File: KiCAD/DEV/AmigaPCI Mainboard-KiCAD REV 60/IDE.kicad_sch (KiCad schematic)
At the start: 55 parts, among them CN900 PRIMARY IDE, CN901 SECONDARY IDE, Q900 MMBT3906, U220 74LVC08, U815 74LVC08, U900 74LVC245, U901 74LVC245, U902 74LVC245, U903 74LVC245, U904 74LVC245, U905 74LVC245, U906 74LVC373, U907 74LVC373

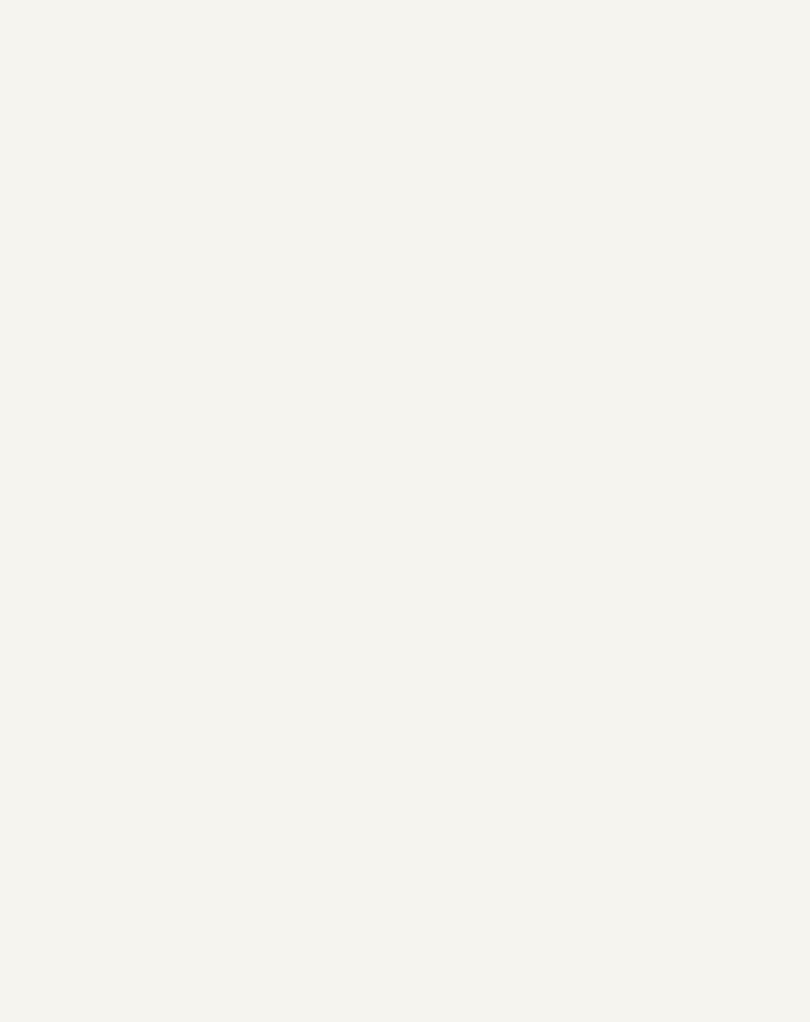
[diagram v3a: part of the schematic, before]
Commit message: Rev 6.0 APCI Work
Added ATA address lines to U110.
Cleaned up some routing.
Removed address lines from U109 - we can pick them up from the AD bus.
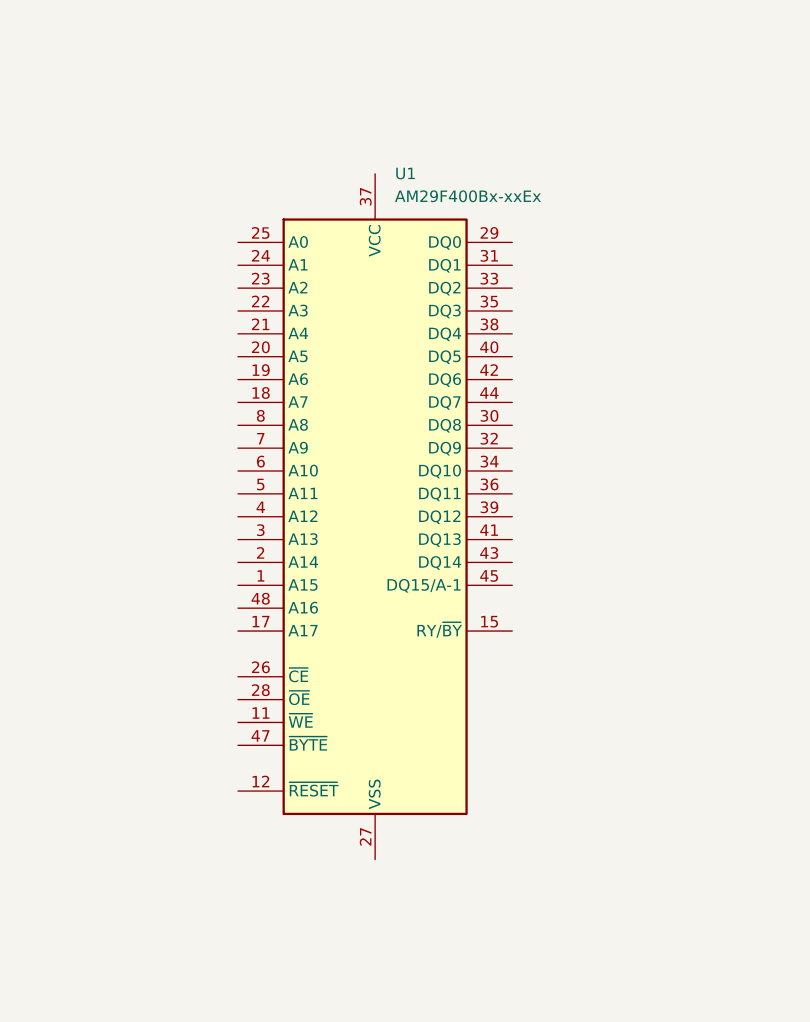
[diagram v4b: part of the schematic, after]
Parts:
- added U1: AM29F400Bx-xxEx, Package_SO:TSOP-I-48_18.4x12mm_P0.5mm, symbol Memory_Flash:AM29F400Bx-xxEx
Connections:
- new net: U1.27 (VSS), U1.46 (VSS)
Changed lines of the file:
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@@
+	)
+	(symbol
+		(lib_id "Memory_Flash:AM29F400Bx-xxEx")
+		(at 278.13 172.72 0)
+		(unit 1)
+		(exclude_from_sim no)
+		(in_bom yes)
+		(on_board yes)
+		(dnp no)
+		(fields_autoplaced yes)
+		(property "Reference" "U1"
+			(at 280.3241 134.62 0)
+			(effects
+				(font
+					(size 1.27 1.27)
+				)
+				(justify left)
+			)
+		)
+		(property "Value" "AM29F400Bx-xxEx"
+			(at 280.3241 137.16 0)
+			(effects
+				(font
+					(size 1.27 1.27)
+				)
+				(justify left)
+			)
+		)
+		(property "Footprint" "Package_SO:TSOP-I-48_18.4x12mm_P0.5mm"
+			(at 278.13 172.72 0)
+			(effects
+				(font
+					(size 1.27 1.27)
+				)
+				(hide yes)
+			)
+		)
+		(property "Datasheet" "https://www.mouser.com/datasheet/2/380/AM29F400B_EOL_21505e8-9219.pdf"
+			(at 277.622 172.72 0)
+			(effects
+				(font
+					(size 1.27 1.27)
+				)
+				(hide yes)
+			)
+		)
+		(property "Description" "4-Mbit (512k x 8-bit / 256k x 16-bit) CMOS 5.0 Volt-only Boot Sector Flash Memory, TSOP-48"
+			(at 277.876 172.72 0)
+			(effects
+				(font
+					(size 1.27 1.27)
+				)
+				(hide yes)
+			)
+		)
+		(pin "46"
+		)
+		(pin "38"
+		)
+		(pin "44"
+		)
+		(pin "25"
+		)
+		(pin "5"
+		)
+		(pin "28"
+		)
+		(pin "33"
+		)
+		(pin "1"
+		)
+		(pin "29"
+		)
+		(pin "47"
+		)
+		(pin "37"
+		)
+		(pin "32"
+		)
+		(pin "3"
+		)
+		(pin "26"
+		)
+		(pin "40"
+		)
+		(pin "21"
+		)
+		(pin "20"
+		)
+		(pin "43"
+		)
+		(pin "39"
+		)
+		(pin "23"
+		)
+		(pin "11"
+		)
+		(pin "41"
+		)
+		(pin "8"
+		)
+		(pin "27"
+		)
+		(pin "6"
+		)
+		(pin "45"
+		)
+		(pin "24"
+		)
+		(pin "9"
+		)
+		(pin "4"
+		)
+		(pin "16"
+		)
+		(pin "19"
+		)
+		(pin "2"
+		)
+		(pin "48"
+		)
+		(pin "31"
+		)
+		(pin "34"
+		)
+		(pin "10"
+		)
+		(pin "22"
+		)
+		(pin "35"
+		)
+		(pin "15"
+		)
+		(pin "18"
+		)
+		(pin "36"
+		)
+		(pin "13"
+		)
+		(pin "30"
+		)
+		(pin "42"
+		)
+		(pin "12"
+		)
+		(pin "7"
+		)
+		(pin "17"
+		)
+		(pin "14"
+		)
+		(instances
+			(project ""
+				(path "/72453515-27fe-4336-91f3-e3c8054f7767/7a35a97e-5686-44dd-976e-0306b0eb5ef2"
+					(reference "U1")
+					(unit 1)
+				)
+			)
+		)
 	)
 	(symbol

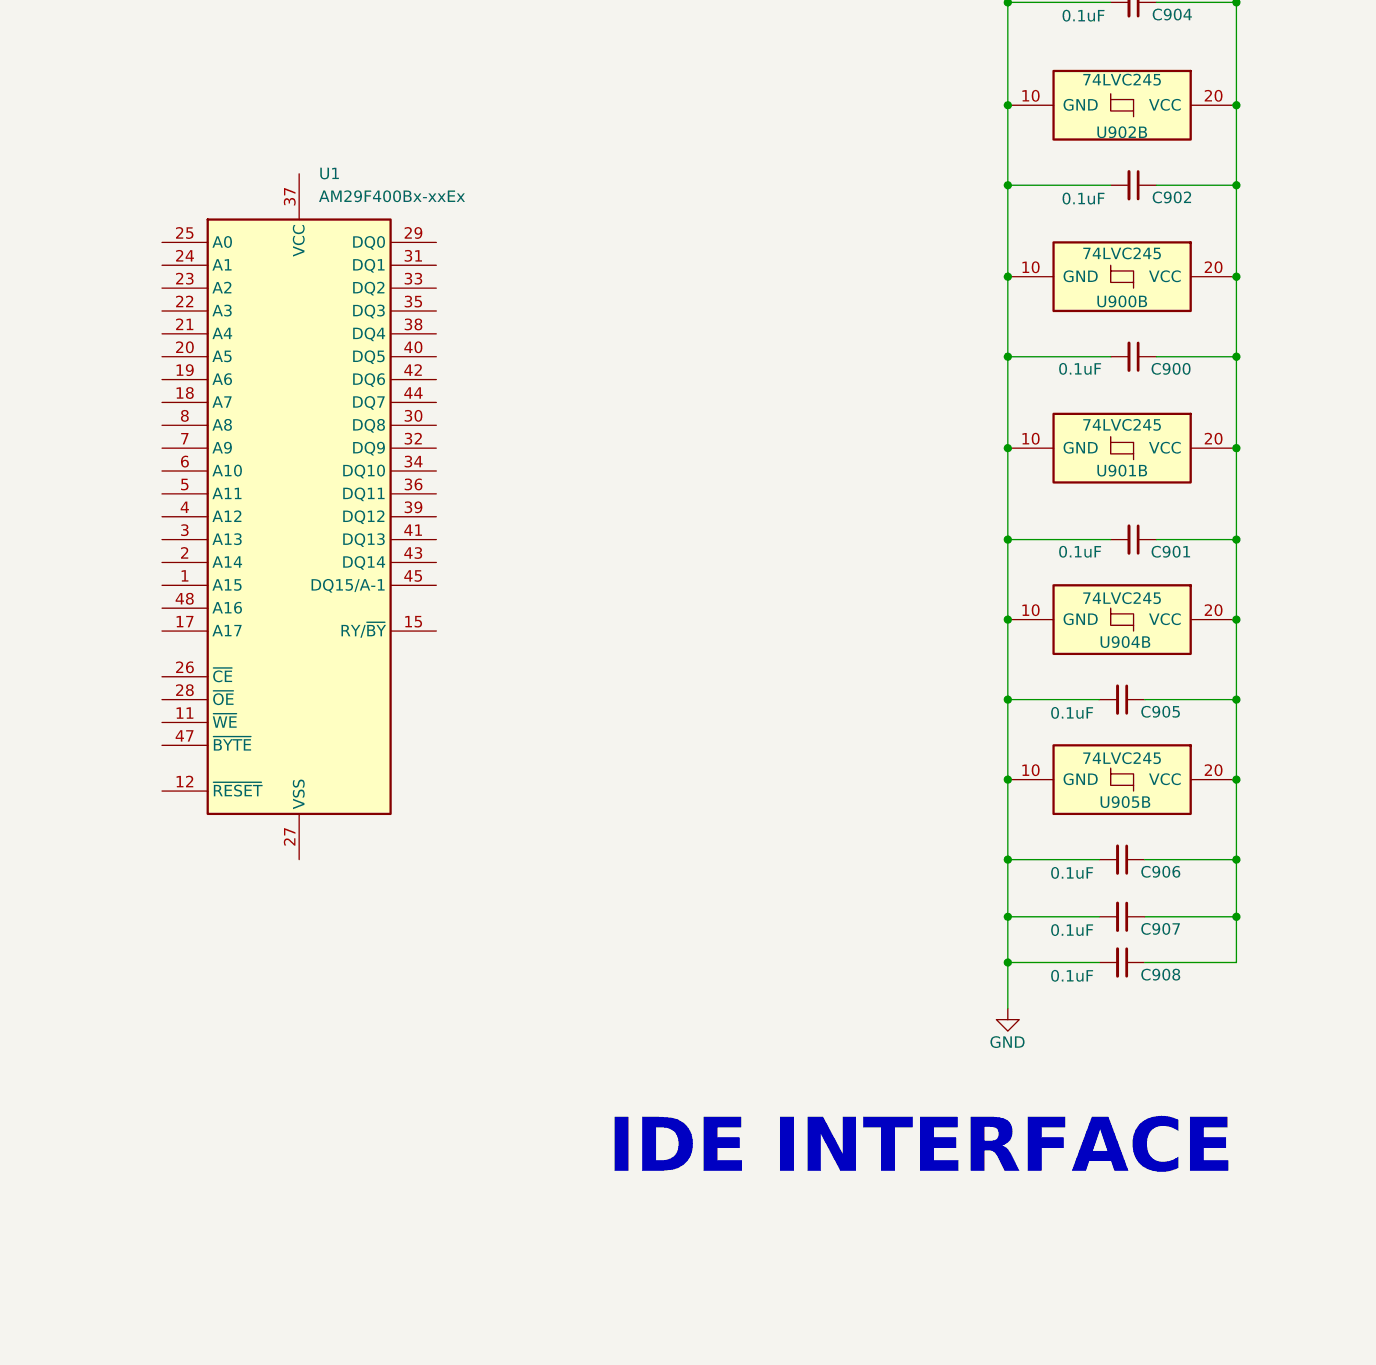
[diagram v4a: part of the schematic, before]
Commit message: Add flash and remove HID buffer.
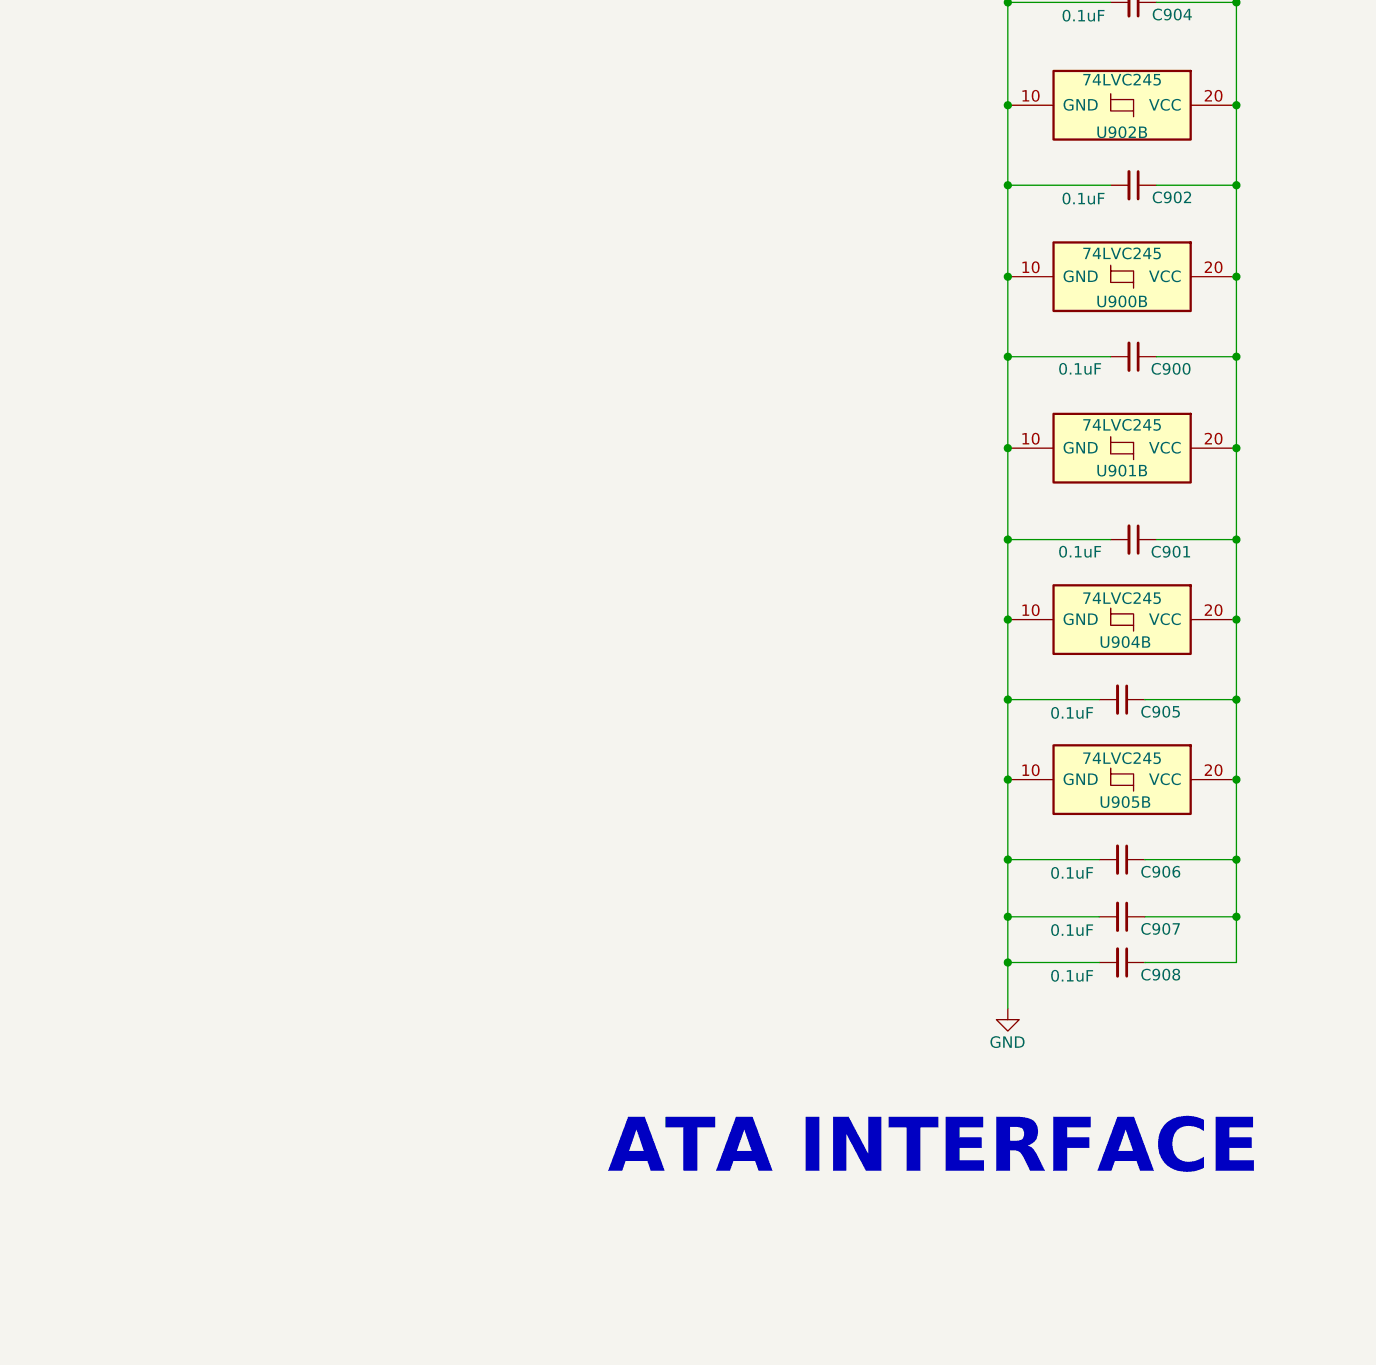
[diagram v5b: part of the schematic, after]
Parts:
- removed U1: AM29F400Bx-xxEx, Package_SO:TSOP-I-48_18.4x12mm_P0.5mm, symbol Memory_Flash:AM29F400Bx-xxEx
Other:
- note added: "ATA INTERFACE"
- note removed: "IDE INTERFACE"
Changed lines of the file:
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@@
 	(title_block
 		(title "AMIGA PCI")
-		(date "2025-05-27")
+		(date "2025-06-26")
 		(rev "6.0")
 	)
@@
 		)
 	)
-	(text "IDE INTERFACE"
+	(text "ATA INTERFACE"
 		(exclude_from_sim no)
 		(at 312.42 246.38 0)
@@
 					(unit 1)
 				)
-			)
-		)
-	)
-	(symbol
-		(lib_id "Memory_Flash:AM29F400Bx-xxEx")
-		(at 278.13 172.72 0)
-		(unit 1)
-		(exclude_from_sim no)
-		(in_bom yes)
-		(on_board yes)
-		(dnp no)
-		(fields_autoplaced yes)
-		(property "Reference" "U1"
-			(at 280.3241 134.62 0)
-			(effects
-				(font
-					(size 1.27 1.27)
-				)
-				(justify left)
-			)
-		)
-		(property "Value" "AM29F400Bx-xxEx"
-			(at 280.3241 137.16 0)
-			(effects
-				(font
-					(size 1.27 1.27)
-				)
-				(justify left)
-			)
-		)
-		(property "Footprint" "Package_SO:TSOP-I-48_18.4x12mm_P0.5mm"
-			(at 278.13 172.72 0)
-			(effects
-				(font
-					(size 1.27 1.27)
-				)
-				(hide yes)
-			)
-		)
-		(property "Datasheet" "https://www.mouser.com/datasheet/2/380/AM29F400B_EOL_21505e8-9219.pdf"
-			(at 277.622 172.72 0)
-			(effects
-				(font
-					(size 1.27 1.27)
-				)
-				(hide yes)
-			)
-		)
-		(property "Description" "4-Mbit (512k x 8-bit / 256k x 16-bit) CMOS 5.0 Volt-only Boot Sector Flash Memory, TSOP-48"
-			(at 277.876 172.72 0)
-			(effects
-				(font
-					(size 1.27 1.27)
-				)
-				(hide yes)
-			)
-		)
-		(pin "46"
-		)
-		(pin "38"
-		)
-		(pin "44"
-		)
-		(pin "25"
-		)
-		(pin "5"
-		)
-		(pin "28"
-		)
-		(pin "33"
-		)
-		(pin "1"
-		)
-		(pin "29"
-		)
-		(pin "47"
-		)
-		(pin "37"
-		)
-		(pin "32"
-		)
-		(pin "3"
-		)
-		(pin "26"
-		)
-		(pin "40"
-		)
-		(pin "21"
-		)
-		(pin "20"
-		)
-		(pin "43"
-		)
-		(pin "39"
-		)
-		(pin "23"
-		)
-		(pin "11"
-		)
-		(pin "41"
-		)
-		(pin "8"
-		)
-		(pin "27"
-		)
-		(pin "6"
-		)
-		(pin "45"
-		)
-		(pin "24"
-		)
-		(pin "9"
-		)
-		(pin "4"
-		)
-		(pin "16"
-		)
-		(pin "19"
-		)
-		(pin "2"
-		)
-		(pin "48"
-		)
-		(pin "31"
-		)
-		(pin "34"
-		)
-		(pin "10"
-		)
-		(pin "22"
-		)
-		(pin "35"
-		)
-		(pin "15"
-		)
-		(pin "18"
-		)
-		(pin "36"
-		)
-		(pin "13"
-		)
-		(pin "30"
-		)
-		(pin "42"
-		)
-		(pin "12"
-		)
-		(pin "7"
-		)
-		(pin "17"
-		)
-		(pin "14"
-		)
-		(instances
-			(project ""
-				(path "/72453515-27fe-4336-91f3-e3c8054f7767/7a35a97e-5686-44dd-976e-0306b0eb5ef2"
-					(reference "U1")
-					(unit 1)
-				)
